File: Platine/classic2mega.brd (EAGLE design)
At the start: 68 x 46 mm, 31 parts, among them IC1 MEGA16-A, IC2 74HC157D, Q2 16MHz, X2 NEB21R

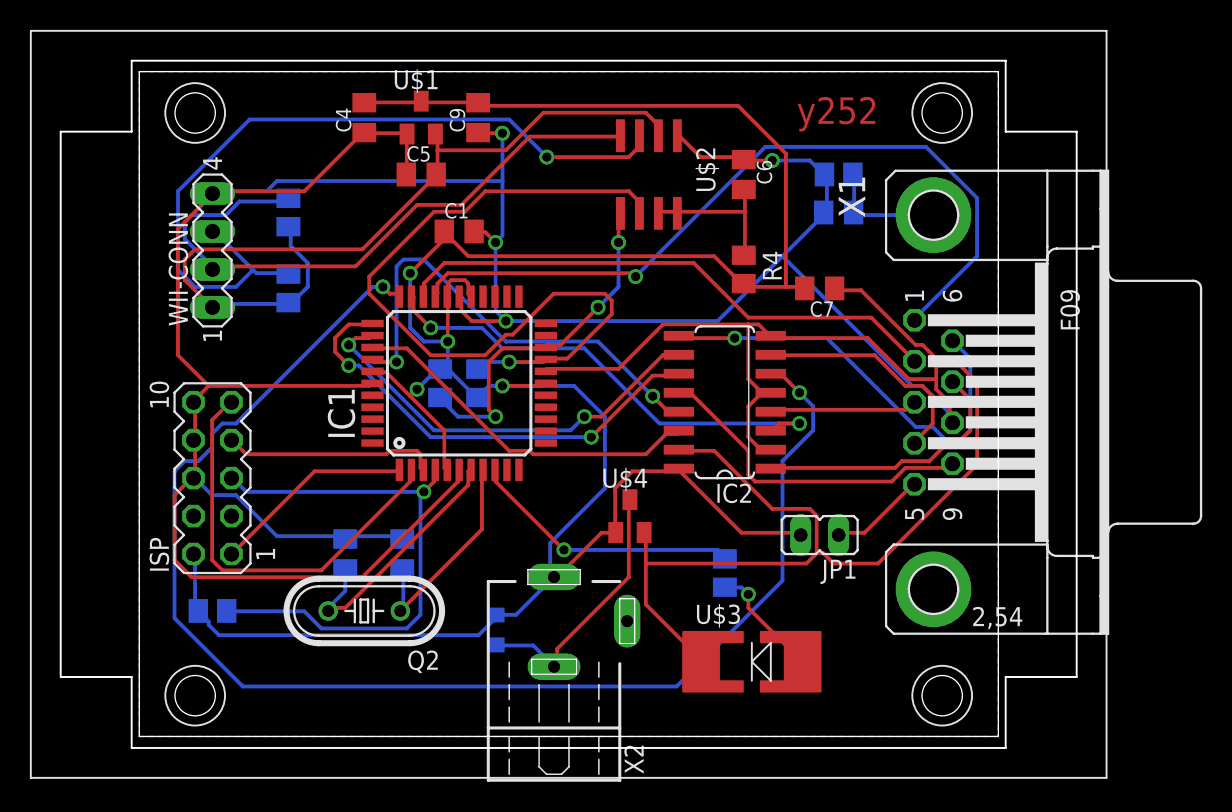
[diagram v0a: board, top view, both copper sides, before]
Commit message: Add "y252" string to backside copper
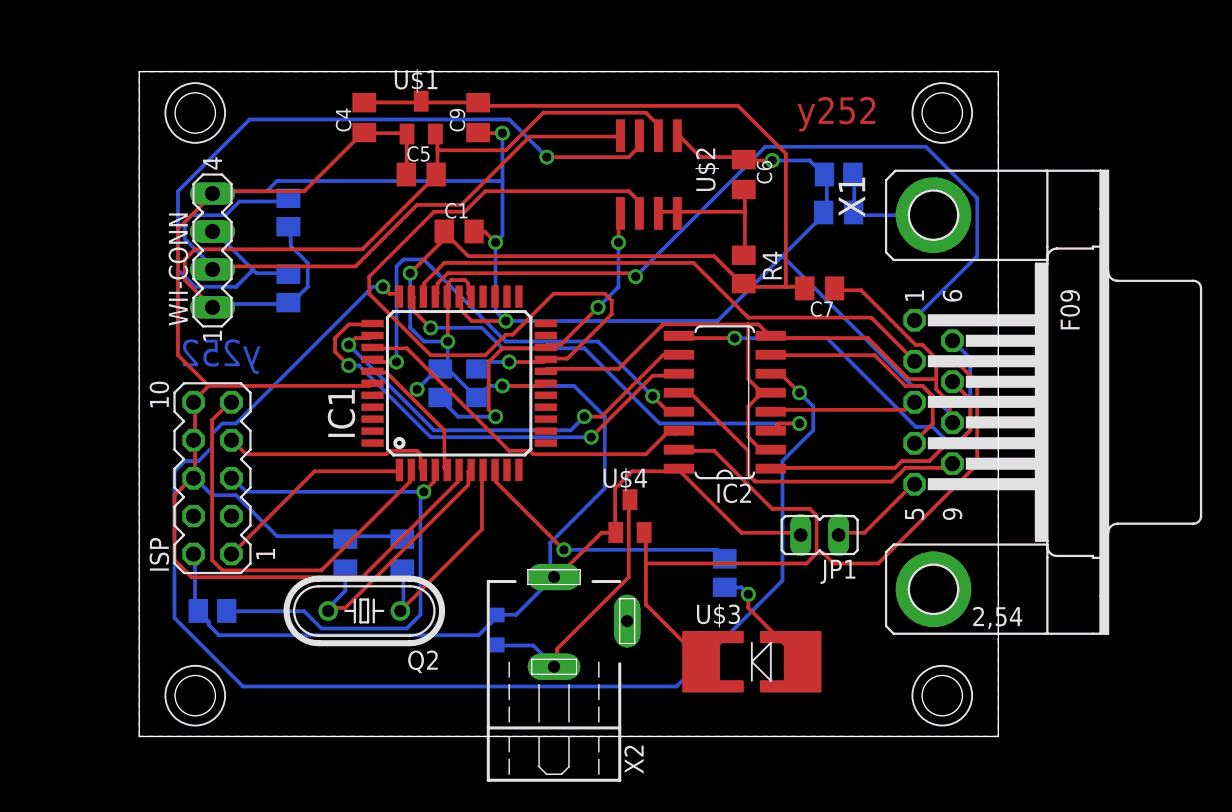
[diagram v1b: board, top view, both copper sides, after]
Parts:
- removed U$5: (no value), case:G028
- added U$6: (no value), case_holes:G028-HOLES
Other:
- board size 68 x 46 mm -> 57.5 x 44.5 mm
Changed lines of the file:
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@@
 <setting verticaltext="up"/>
 </settings>
-<grid distance="0.5" unitdist="mm" unit="mm" style="lines" multiple="1" display="no" altdistance="0.025" altunitdist="inch" altunit="inch"/>
+<grid distance="0.003125" unitdist="mic" unit="mm" style="lines" multiple="1" display="no" altdistance="0.025" altunitdist="inch" altunit="inch"/>
 <layers>
 <layer number="1" name="Top" color="4" fill="1" visible="yes" active="yes"/>
@@
 <wire x1="20.5" y1="61.5" x2="20.5" y2="17" width="0" layer="20"/>
 <text x="64.5" y="58" size="1.778" layer="1" font="vector" ratio="15">y252</text>
+<text x="28.679425" y="41.780425" size="1.778" layer="16" font="vector" ratio="15" rot="MR0">y252</text>
 </plain>
 <attributes>
@@
 <element name="U$4" library="TSM2310" package="SOT23" value="TSM2310" x="53.34" y="31.75"/>
 <element name="R9" library="varistor" package="CT/CN0603" value="EZJZ1V120KA" x="44.45" y="24.13" rot="MR270"/>
-<element name="U$5" library="case" package="G028" value="" x="15.24" y="62.23"/>
 <element name="U$3" library="VLMC310" package="PLCC-2" value="VLMC310" x="61.5" y="22"/>
+<element name="U$6" library="case_holes" package="G028-HOLES" value="" x="15.245190625" y="62.230759375"/>
 </elements>
 <signals>
